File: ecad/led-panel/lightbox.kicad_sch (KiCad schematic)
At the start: 20 parts, among them J3 Conn_01x03_Pin, P1 USB_C_Plug_USB2.0, SW1 RST, SW2 BOOT, SW3 USER1, SW4 USER2, U1 ESP32-S3-WROOM-1, U2 AMS1117-3.3, U3 SN74LVC1T45DBV

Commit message: remove USB C port, using JST-XH connector to breakout board instead; add testpoints; switch from 2 gnd planes to 1 5V plane and 1 gnd plane; prelim routing complete
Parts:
- removed D+1, D-1: TestPoint, symbol Connector:TestPoint
- removed J3: Conn_01x03_Pin, symbol Connector:Conn_01x03_Pin
- removed P1: USB_C_Plug_USB2.0, Connector_USB:USB_C_Receptacle_HRO_TYPE-C-31-M-17, symbol Connector:USB_C_Plug_USB2.0
- removed R2, R3: 5.1k, Resistor_SMD:R_0805_2012Metric, symbol Device:R
- added 3V3: TestPoint, TestPoint:TestPoint_Pad_D2.0mm, symbol Connector:TestPoint
- added PRGM1, PWR1: Conn_01x04, Connector_JST:JST_XH_B4B-XH-AM_1x04_P2.50mm_Vertical, symbol Connector_Generic:Conn_01x04
- LED_GPIO1: footprint (none) -> TestPoint:TestPoint_Pad_D2.0mm
- SW1, SW2: footprint Button_Switch_THT:SW_PUSH_6mm -> Button_Switch_SMD:SW_SPST_TS-1088-xR020
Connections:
- net +3V3: now also 3V3.1
- net +5V: now also PWR1.1 (Pin_1)
- net D+: now also PRGM1.3 (Pin_3)
- net D-: now also PRGM1.2 (Pin_2)
- net GND: now also PRGM1.4 (Pin_4), PWR1.4 (Pin_4)
- no-connect marks 6 -> 8

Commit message: before splitting into 2 boards
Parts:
- added IO15, IO16, IO17, IO18, IO38, IO39, IO4, IO40, IO41, IO42, IO5, IO6, IO7, IO8: TestPoint, TestPoint:TestPoint_Pad_D1.5mm, symbol Connector:TestPoint
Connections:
- net at U1.10 (IO17): now also IO17.1
- net at U1.11 (IO18): now also IO18.1
- net at U1.12 (IO8): now also IO8.1
- net at U1.31 (IO38): now also IO38.1
- net at U1.32 (IO39): now also IO39.1
- net at U1.33 (IO40): now also IO40.1
- net at U1.34 (IO41): now also IO41.1
- net at U1.35 (IO42): now also IO42.1
- net at U1.4 (IO4): now also IO4.1
- net at U1.5 (IO5): now also IO5.1
- net at U1.6 (IO6): now also IO6.1
- net at U1.7 (IO7): now also IO7.1
- net at U1.8 (IO15): now also IO15.1
- net at U1.9 (IO16): now also IO16.1
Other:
- moved on the sheet: LED_GPIO1

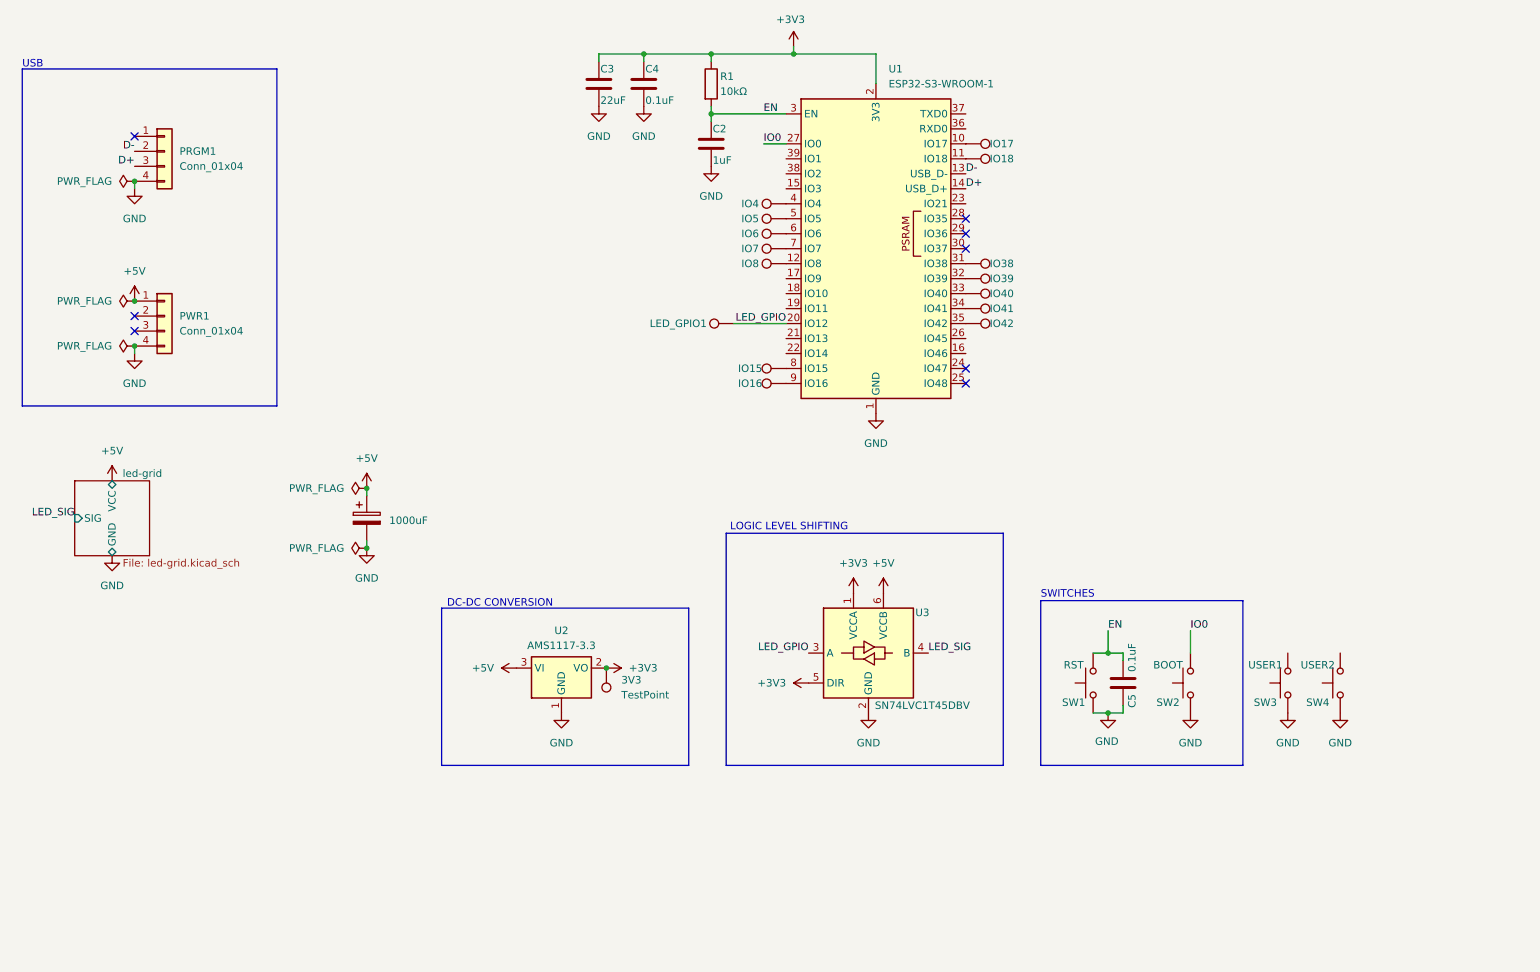
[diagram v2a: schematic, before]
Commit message: split into 2 boards; switch led panel from 4 layers to 2 layers;
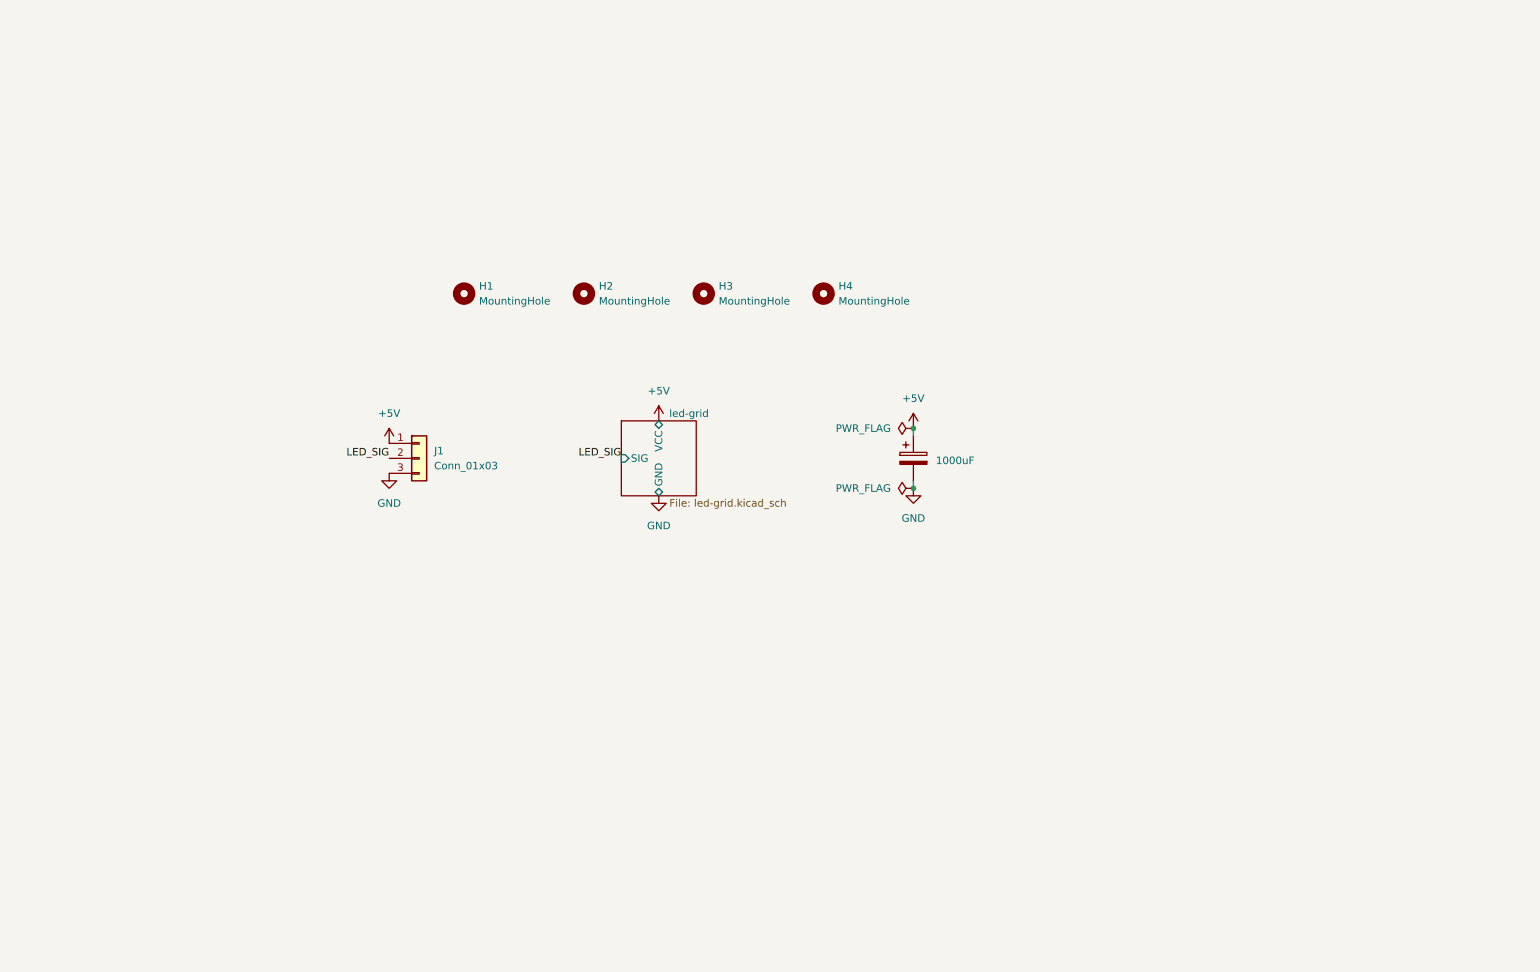
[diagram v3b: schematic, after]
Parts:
- removed 3V3, LED_GPIO1: TestPoint, TestPoint:TestPoint_Pad_D2.0mm, symbol Connector:TestPoint
- removed C2: 1uF, Capacitor_SMD:C_0805_2012Metric, symbol Device:C
- removed C3: 22uF, Capacitor_SMD:C_0805_2012Metric, symbol Device:C
- removed C4, C5: 0.1uF, Capacitor_SMD:C_0805_2012Metric, symbol Device:C
- removed IO15, IO16, IO17, IO18, IO38, IO39, IO4, IO40, IO41, IO42, IO5, IO6, IO7, IO8: TestPoint, TestPoint:TestPoint_Pad_D1.5mm, symbol Connector:TestPoint
- removed PRGM1, PWR1: Conn_01x04, Connector_JST:JST_XH_B4B-XH-AM_1x04_P2.50mm_Vertical, symbol Connector_Generic:Conn_01x04
- removed R1: 10kΩ, Resistor_SMD:R_0805_2012Metric, symbol Device:R
- removed SW1: RST, Button_Switch_SMD:SW_SPST_TS-1088-xR020, symbol Switch:SW_Push
- removed SW2: BOOT, Button_Switch_SMD:SW_SPST_TS-1088-xR020, symbol Switch:SW_Push
- removed SW3: USER1, Button_Switch_THT:SW_PUSH_6mm, symbol Switch:SW_Push
- removed SW4: USER2, Button_Switch_THT:SW_PUSH_6mm, symbol Switch:SW_Push
- removed U1: ESP32-S3-WROOM-1, RF_Module:ESP32-S3-WROOM-1, symbol RF_Module:ESP32-S3-WROOM-1
- removed U2: AMS1117-3.3, Package_TO_SOT_SMD:SOT-223-3_TabPin2, symbol Regulator_Linear:AMS1117-3.3
- removed U3: SN74LVC1T45DBV, Package_TO_SOT_SMD:SOT-23-6, symbol Logic_LevelTranslator:SN74LVC1T45DBV
- added H1, H2, H3, H4: MountingHole, MountingHole:MountingHole_3.2mm_M3_Pad, symbol Mechanical:MountingHole
- added J1: Conn_01x03, Connector_JST:JST_XH_B3B-XH-AM_1x03_P2.50mm_Vertical, symbol Connector_Generic:Conn_01x03
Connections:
- net +5V: now also J1.1 (Pin_1)
- net GND: now also J1.3 (Pin_3)
- net LED_SIG: now also J1.2 (Pin_2)
- no-connect marks 8 -> 0
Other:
- note removed: "DC-DC CONVERSION"
- note removed: "LOGIC LEVEL SHIFTING"
- note removed: "SWITCHES"
- note removed: "USB"

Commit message: added vertical USB-C connector to controller board; and possibly much more
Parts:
- H1, H2, H3, H4: footprint MountingHole:MountingHole_3.2mm_M3_Pad -> MountingHole:MountingHole_4.3mm_M4_Pad
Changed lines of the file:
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@@
 			)
 		)
-		(property "Footprint" "MountingHole:MountingHole_3.2mm_M3_Pad"
+		(property "Footprint" "MountingHole:MountingHole_4.3mm_M4_Pad"
 			(at 113.03 69.85 0)
 			(hide yes)
@@
 			)
 		)
-		(property "Footprint" "MountingHole:MountingHole_3.2mm_M3_Pad"
+		(property "Footprint" "MountingHole:MountingHole_4.3mm_M4_Pad"
 			(at 133.35 69.85 0)
 			(hide yes)
@@
 			)
 		)
-		(property "Footprint" "MountingHole:MountingHole_3.2mm_M3_Pad"
+		(property "Footprint" "MountingHole:MountingHole_4.3mm_M4_Pad"
 			(at 92.71 69.85 0)
 			(hide yes)
@@
 			)
 		)
-		(property "Footprint" "MountingHole:MountingHole_3.2mm_M3_Pad"
+		(property "Footprint" "MountingHole:MountingHole_4.3mm_M4_Pad"
 			(at 153.67 69.85 0)
 			(hide yes)

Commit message: prelim checks of led panel
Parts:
- H1, H2, H3, H4: footprint MountingHole:MountingHole_4.3mm_M4_Pad -> MountingHole:MountingHole_4.3mm_M4
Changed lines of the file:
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@@
 			)
 		)
-		(property "Footprint" "MountingHole:MountingHole_4.3mm_M4_Pad"
+		(property "Footprint" "MountingHole:MountingHole_4.3mm_M4"
 			(at 113.03 69.85 0)
 			(hide yes)
@@
 			)
 		)
-		(property "Footprint" "MountingHole:MountingHole_4.3mm_M4_Pad"
+		(property "Footprint" "MountingHole:MountingHole_4.3mm_M4"
 			(at 133.35 69.85 0)
 			(hide yes)
@@
 			)
 		)
-		(property "Footprint" "MountingHole:MountingHole_4.3mm_M4_Pad"
+		(property "Footprint" "MountingHole:MountingHole_4.3mm_M4"
 			(at 92.71 69.85 0)
 			(hide yes)
@@
 			)
 		)
-		(property "Footprint" "MountingHole:MountingHole_4.3mm_M4_Pad"
+		(property "Footprint" "MountingHole:MountingHole_4.3mm_M4"
 			(at 153.67 69.85 0)
 			(hide yes)

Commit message: populate BOM fields with MPN and LCSC Part #
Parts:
- C1: LCSC# (none) -> C72470; MPN (none) -> RVT1C102M1010
- J1: LCSC# (none) -> C144394; MPN (none) -> B3B-XH-A(LF)(SN)
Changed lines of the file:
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@@
+			)
+		)
+		(property "LCSC#" "C144394"
+			(at 85.09 97.79 0)
+			(hide yes)
+			(show_name no)
+			(do_not_autoplace no)
+			(effects
+				(font
+					(size 1.27 1.27)
+				)
+			)
+		)
+		(property "MPN" "B3B-XH-A(LF)(SN)"
+			(at 85.09 97.79 0)
+			(hide yes)
+			(show_name no)
+			(do_not_autoplace no)
+			(effects
+				(font
+					(size 1.27 1.27)
+				)
 			)
 		)
@@
 			)
 		)
+		(property "LCSC#" ""
+			(at 113.03 69.85 0)
+			(hide yes)
+			(show_name no)
+			(do_not_autoplace no)
+			(effects
+				(font
+					(size 1.27 1.27)
+				)
+			)
+		)
+		(property "MPN" ""
+			(at 113.03 69.85 0)
+			(hide yes)
+			(show_name no)
+			(do_not_autoplace no)
+			(effects
+				(font
+					(size 1.27 1.27)
+				)
+			)
+		)
 		(instances
 			(project "lightbox"
@@
 			)
 		)
+		(property "LCSC#" "C72470"
+			(at 168.91 97.79 0)
+			(hide yes)
+			(show_name no)
+			(do_not_autoplace no)
+			(effects
+				(font
+					(size 1.27 1.27)
+				)
+			)
+		)
+		(property "MPN" "RVT1C102M1010"
+			(at 168.91 97.79 0)
+			(hide yes)
+			(show_name no)
+			(do_not_autoplace no)
+			(effects
+				(font
+					(size 1.27 1.27)
+				)
+			)
+		)
 		(pin "2"
 		)
@@
 			)
 		)
+		(property "LCSC#" ""
+			(at 133.35 69.85 0)
+			(hide yes)
+			(show_name no)
+			(do_not_autoplace no)
+			(effects
+				(font
+					(size 1.27 1.27)
+				)
+			)
+		)
+		(property "MPN" ""
+			(at 133.35 69.85 0)
+			(hide yes)
+			(show_name no)
+			(do_not_autoplace no)
+			(effects
+				(font
+					(size 1.27 1.27)
+				)
+			)
+		)
 		(instances
 			(project "lightbox"
@@
 			)
 		)
+		(property "LCSC#" ""
+			(at 92.71 69.85 0)
+			(hide yes)
+			(show_name no)
+			(do_not_autoplace no)
+			(effects
+				(font
+					(size 1.27 1.27)
+				)
+			)
+		)
+		(property "MPN" ""
+			(at 92.71 69.85 0)
+			(hide yes)
+			(show_name no)
+			(do_not_autoplace no)
+			(effects
+				(font
+					(size 1.27 1.27)
+				)
+			)
+		)
 		(instances
 			(project "lightbox"
@@
 			(at 153.67 69.85 0)
 			(hide yes)
+			(show_name no)
+			(do_not_autoplace no)
+			(effects
+				(font
+					(size 1.27 1.27)
+				)
+			)
+		)
+		(property "LCSC#" ""
+			(at 153.67 69.85 0)
+			(hide yes)
+			(show_name no)
+			(do_not_autoplace no)
+			(effects
+				(font
+					(size 1.27 1.27)
+				)
+			)
+		)
+		(property "MPN" ""
+			(at 153.67 69.85 0)
+			(hide yes)

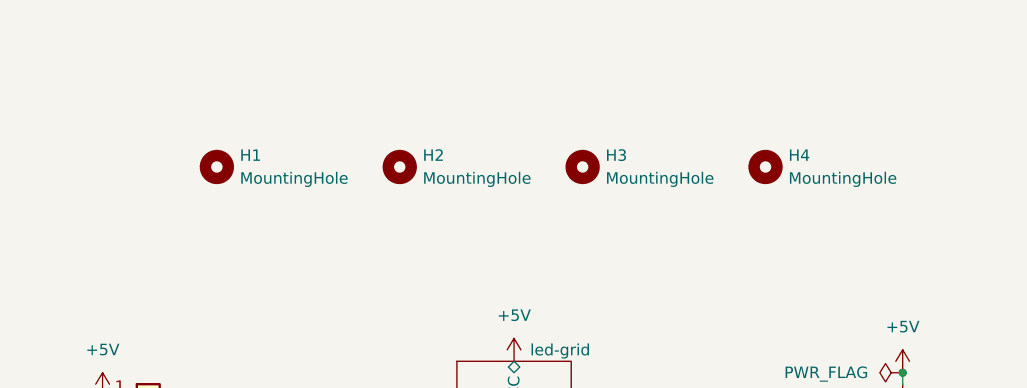
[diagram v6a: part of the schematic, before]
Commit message: final design review for v1 order; reroute some components; add LED to controller
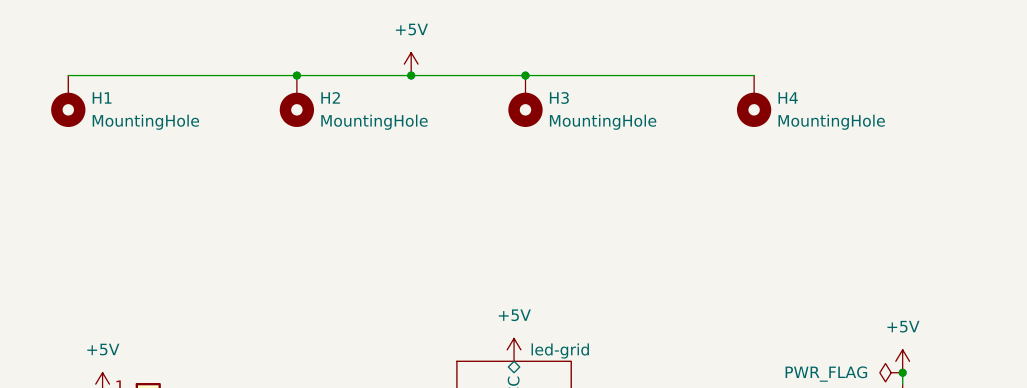
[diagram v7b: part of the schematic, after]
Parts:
- H1, H2, H3, H4: footprint MountingHole:MountingHole_4.3mm_M4 -> MountingHole:MountingHole_4.3mm_M4_ISO7380_Pad_TopOnly; symbol Mechanical:MountingHole -> Mechanical:MountingHole_Pad
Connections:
- net +5V: now also H1.1, H2.1, H3.1, H4.1
